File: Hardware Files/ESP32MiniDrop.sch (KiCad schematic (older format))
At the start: 51 parts, among them J1 USB_B_Mini, J2 Barrel_Jack, J3 AudioJack3, J4 Solenoid1 Terminal, J5 0.100\" 2x4 Header, M1 Conn_01x01, M2 Conn_01x01, M3 Conn_01x01, M4 Conn_01x01, Q1 S8050, Q2 S8050, Q3 NMOS 60V 46A, SW1 SPST (RED), SW2 SPST (BLUE), U1 CP2102N-A01-GQFN28, U2 AZ1117-3.3, U3 ESP32-WROOM-32, U4 4N25, U5 4N25

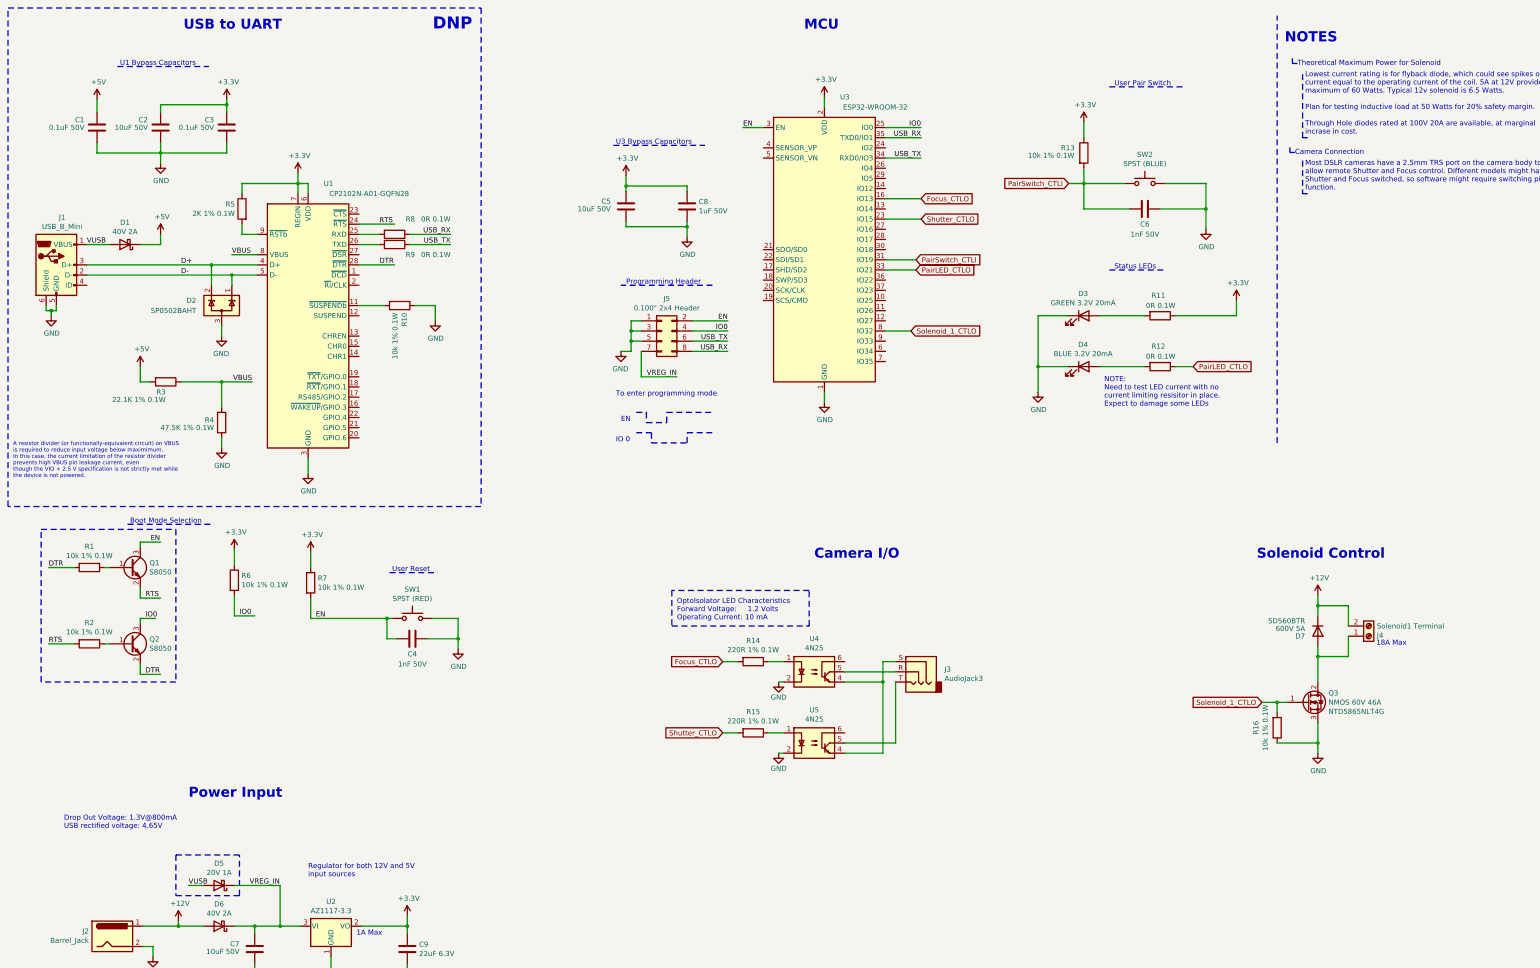
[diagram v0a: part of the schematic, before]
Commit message: Remove USB to UART components
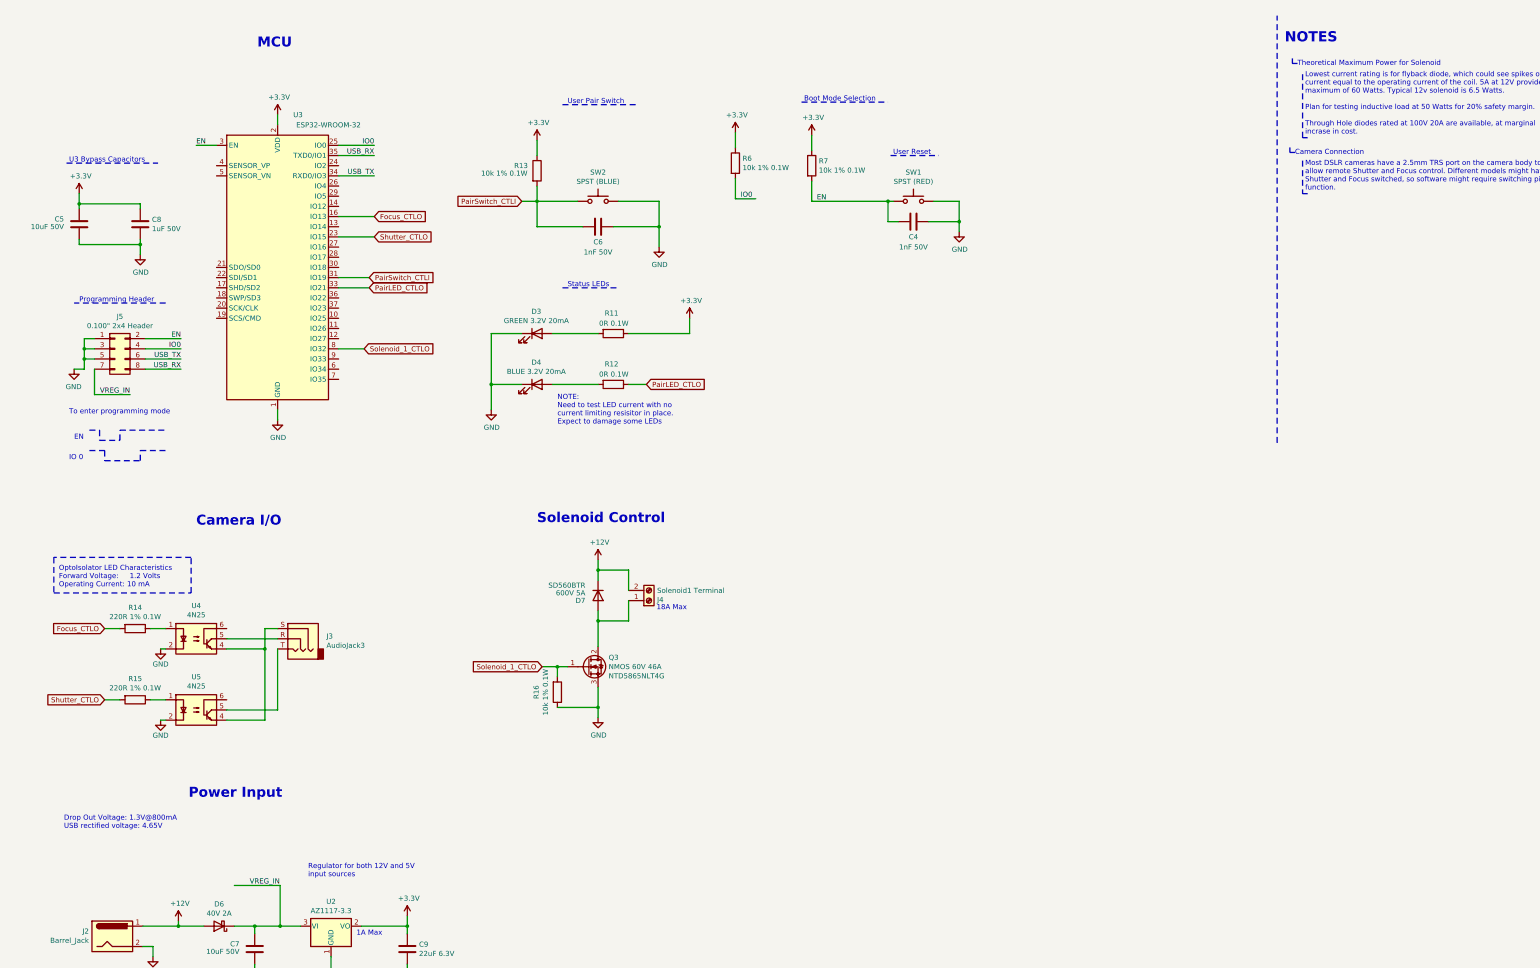
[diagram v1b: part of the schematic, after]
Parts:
- removed C1, C3: 0.1uF 50V, Capacitor_SMD:C_0603_1608Metric_Pad1.05x0.95mm_HandSolder, symbol Device:C
- removed C2: 10uF 50V, Capacitor_SMD:C_1206_3216Metric_Pad1.42x1.75mm_HandSolder, symbol Device:C
- removed D1: 40V 2A, Diode_SMD:D_SOD-123F, symbol Diode:1N5819
- removed D2: SP0502BAHT, Package_TO_SOT_SMD:SOT-23, symbol Power_Protection:SP0502BAHT
- removed D5: 20V 1A, Diode_SMD:D_SOD-123F, symbol Diode:1N5819
- removed J1: USB_B_Mini, ESP32 Drop Controller:USB_Micro-B_Molex-105017-0001_3D, symbol Connector:USB_B_Mini
- removed Q1, Q2: S8050, Package_TO_SOT_SMD:SOT-23, symbol Device:Q_NPN_BEC
- removed R1, R10, R2: 10k 1% 0.1W, Resistor_SMD:R_0603_1608Metric_Pad1.05x0.95mm_HandSolder, symbol Device:R
- removed R3: 22.1K 1% 0.1W, Resistor_SMD:R_0603_1608Metric_Pad1.05x0.95mm_HandSolder, symbol Device:R
- removed R4: 47.5K 1% 0.1W, Resistor_SMD:R_0603_1608Metric_Pad1.05x0.95mm_HandSolder, symbol Device:R
- removed R5: 2K 1% 0.1W, Resistor_SMD:R_0603_1608Metric_Pad1.05x0.95mm_HandSolder, symbol Device:R
- removed R8, R9: 0R 0.1W, Resistor_SMD:R_0603_1608Metric_Pad1.05x0.95mm_HandSolder, symbol Device:R
- removed U1: CP2102N-A01-GQFN28, Package_DFN_QFN:QFN-28-1EP_5x5mm_P0.5mm_EP3.35x3.35mm, symbol Interface_USB:CP2102N-A01-GQFN28
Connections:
- net labels removed: +5V, D+, D-, DTR, RTS, VBUS, VUSB
- wire segments 184 -> 120
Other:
- note removed: "A resistor divider (or functionally-equivalent circuit) on VBUS\nis required to reduce input voltage below maximimum. \nIn this case, the current limitation of the resistor divider \nprevents high VBUS pin leakage current, even \nthough the VIO + 2.5 V specification is not strictly met while\nthe device is not powered."
- note removed: "DNP"
- note removed: "U1 Bypass Capacitors"
- note removed: "USB to UART"
- moved on the sheet: C4, C5, C6, C8, D3, D4, D7, J3, J4, J5, Q3, R11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

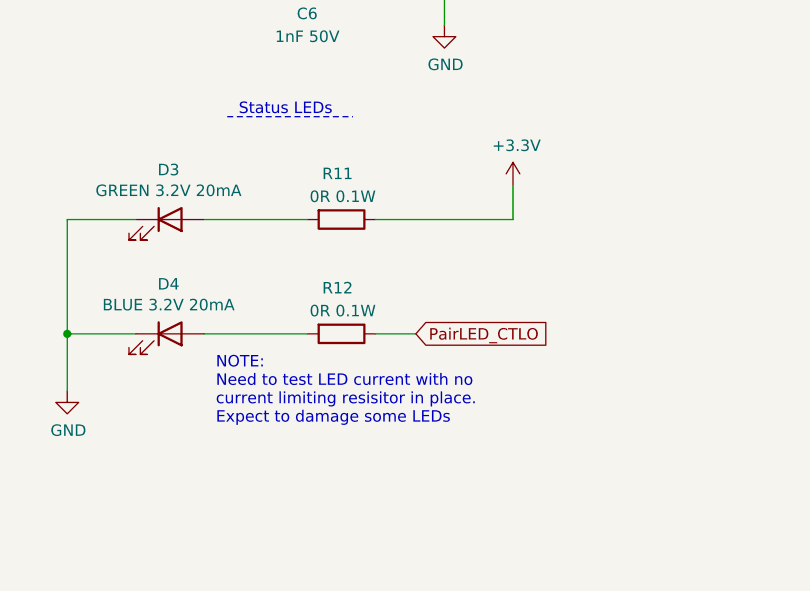
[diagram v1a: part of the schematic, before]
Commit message: Update passives to all 1206, unroute and reposition
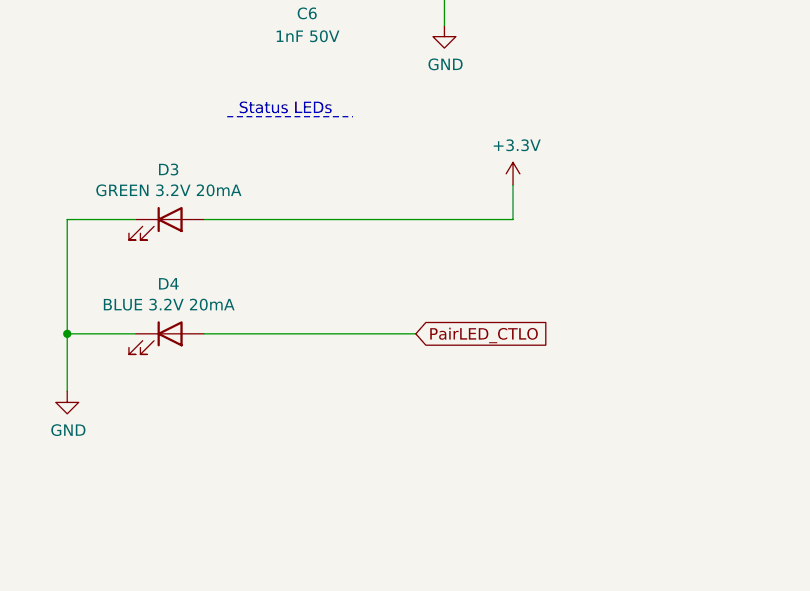
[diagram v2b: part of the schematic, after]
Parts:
- removed R11, R12: 0R 0.1W, Resistor_SMD:R_0603_1608Metric_Pad1.05x0.95mm_HandSolder, symbol Device:R
- C4, C6: footprint Capacitor_SMD:C_0603_1608Metric_Pad1.05x0.95mm_HandSolder -> Capacitor_SMD:C_1206_3216Metric_Pad1.42x1.75mm_HandSolder; MF Yageo -> (none); MPN CC0603KRX7R9BB102 -> (none)
- C8: footprint Capacitor_SMD:C_0603_1608Metric_Pad1.05x0.95mm_HandSolder -> Capacitor_SMD:C_1206_3216Metric_Pad1.42x1.75mm_HandSolder; MF Yageo -> (none); MPN CC0603KRX5R9BB105 -> (none)
- C9: footprint Capacitor_SMD:C_0805_2012Metric_Pad1.15x1.40mm_HandSolder -> Capacitor_SMD:C_1206_3216Metric_Pad1.42x1.75mm_HandSolder; MF Samsung Electro-Mechanics -> (none); MPN CL21A226MQQNNNE -> (none)
- R13, R16, R6, R7: footprint Resistor_SMD:R_0603_1608Metric_Pad1.05x0.95mm_HandSolder -> Resistor_SMD:R_1206_3216Metric_Pad1.42x1.75mm_HandSolder; MPN RC0603FR-0710KL -> (none)
- R14, R15: footprint Resistor_SMD:R_0603_1608Metric_Pad1.05x0.95mm_HandSolder -> Resistor_SMD:R_1206_3216Metric_Pad1.42x1.75mm_HandSolder; MPN RC0603FR-07220RL -> (none)
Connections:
- net +3V3: now also D3.2 (A)
- net PairLED_CTLO: now also D4.2 (A)
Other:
- note removed: "NOTE:\nNeed to test LED current with no\ncurrent limiting resisitor in place.\nExpect to damage some LEDs"
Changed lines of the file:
@@
 F 0 "R16" V 5718 7250 50  0000 C CNN
 F 1 "10k 1% 0.1W" V 5809 7250 50  0000 C CNN
-F 2 "Resistor_SMD:R_0603_1608Metric_Pad1.05x0.95mm_HandSolder" V 5855 7250 50  0001 C CNN
+F 2 "Resistor_SMD:R_1206_3216Metric_Pad1.42x1.75mm_HandSolder" V 5855 7250 50  0001 C CNN
 F 3 "~" H 5925 7250 50  0001 C CNN
 F 4 "Yageo" H 5925 7250 50  0001 C CNN "MF"
-F 5 "RC0603FR-0710KL" H 5925 7250 50  0001 C CNN "MPN"
+F 5 "" H 5925 7250 50  0001 C CNN "MPN"
 	1    5925 7250
 	1    0    0    1
@@
 F 0 "R6" H 7745 2096 50  0000 L CNN
 F 1 "10k 1% 0.1W" H 7745 2005 50  0000 L CNN
-F 2 "Resistor_SMD:R_0603_1608Metric_Pad1.05x0.95mm_HandSolder" V 7605 2050 50  0001 C CNN
+F 2 "Resistor_SMD:R_1206_3216Metric_Pad1.42x1.75mm_HandSolder" V 7605 2050 50  0001 C CNN
 F 3 "~" H 7675 2050 50  0001 C CNN
 F 4 "Yageo" H 7675 2050 50  0001 C CNN "MF"
-F 5 "RC0603FR-0710KL" H 7675 2050 50  0001 C CNN "MPN"
+F 5 "" H 7675 2050 50  0001 C CNN "MPN"
 	1    7675 2050
 	1    0    0    -1
@@
 F 0 "R7" H 8495 2121 50  0000 L CNN
 F 1 "10k 1% 0.1W" H 8495 2030 50  0000 L CNN
-F 2 "Resistor_SMD:R_0603_1608Metric_Pad1.05x0.95mm_HandSolder" V 8355 2075 50  0001 C CNN
+F 2 "Resistor_SMD:R_1206_3216Metric_Pad1.42x1.75mm_HandSolder" V 8355 2075 50  0001 C CNN
 F 3 "~" H 8425 2075 50  0001 C CNN
 F 4 "Yageo" H 8425 2075 50  0001 C CNN "MF"
-F 5 "RC0603FR-0710KL" H 8425 2075 50  0001 C CNN "MPN"
+F 5 "" H 8425 2075 50  0001 C CNN "MPN"
 	1    8425 2075
 	1    0    0    -1
@@
 F 0 "C8" H 1940 2696 50  0000 L CNN
 F 1 "1uF 50V" H 1940 2605 50  0000 L CNN
-F 2 "Capacitor_SMD:C_0603_1608Metric_Pad1.05x0.95mm_HandSolder" H 1863 2500 50  0001 C CNN
+F 2 "Capacitor_SMD:C_1206_3216Metric_Pad1.42x1.75mm_HandSolder" H 1863 2500 50  0001 C CNN
 F 3 "~" H 1825 2650 50  0001 C CNN
-F 4 "Yageo" H 1825 2650 50  0001 C CNN "MF"
-F 5 "CC0603KRX5R9BB105" H 1825 2650 50  0001 C CNN "MPN"
+F 4 "" H 1825 2650 50  0001 C CNN "MF"
+F 5 "" H 1825 2650 50  0001 C CNN "MPN"
 	1    1825 2650
 	1    0    0    -1
@@
 F 0 "C4" V 9575 2625 50  0000 C CNN
 F 1 "1nF 50V" V 9675 2625 50  0000 C CNN
-F 2 "Capacitor_SMD:C_0603_1608Metric_Pad1.05x0.95mm_HandSolder" H 9463 2475 50  0001 C CNN
+F 2 "Capacitor_SMD:C_1206_3216Metric_Pad1.42x1.75mm_HandSolder" H 9463 2475 50  0001 C CNN
 F 3 "~" H 9425 2625 50  0001 C CNN
-F 4 "Yageo" V 9425 2625 50  0001 C CNN "MF"
-F 5 "CC0603KRX7R9BB102" V 9425 2625 50  0001 C CNN "MPN"
+F 4 "" V 9425 2625 50  0001 C CNN "MF"
+F 5 "" V 9425 2625 50  0001 C CNN "MPN"
 	1    9425 2625
 	0    1    1    0
@@
 F 0 "C6" V 6475 2675 50  0000 C CNN
 F 1 "1nF 50V" V 6575 2675 50  0000 C CNN
-F 2 "Capacitor_SMD:C_0603_1608Metric_Pad1.05x0.95mm_HandSolder" H 6363 2525 50  0001 C CNN
+F 2 "Capacitor_SMD:C_1206_3216Metric_Pad1.42x1.75mm_HandSolder" H 6363 2525 50  0001 C CNN
 F 3 "~" H 6325 2675 50  0001 C CNN
-F 4 "Yageo" V 6325 2675 50  0001 C CNN "MF"
-F 5 "CC0603KRX7R9BB102" V 6325 2675 50  0001 C CNN "MPN"
+F 4 "" V 6325 2675 50  0001 C CNN "MF"
+F 5 "" V 6325 2675 50  0001 C CNN "MPN"
 	1    6325 2675
 	0    1    1    0
@@
 F 0 "R13" H 5500 2175 50  0000 L CNN
 F 1 "10k 1% 0.1W" H 5175 2100 50  0000 L CNN
-F 2 "Resistor_SMD:R_0603_1608Metric_Pad1.05x0.95mm_HandSolder" V 5655 2125 50  0001 C CNN
+F 2 "Resistor_SMD:R_1206_3216Metric_Pad1.42x1.75mm_HandSolder" V 5655 2125 50  0001 C CNN
 F 3 "~" H 5725 2125 50  0001 C CNN
 F 4 "Yageo" H 5725 2125 50  0001 C CNN "MF"
-F 5 "RC0603FR-0710KL" H 5725 2125 50  0001 C CNN "MPN"
+F 5 "" H 5725 2125 50  0001 C CNN "MPN"
 	1    5725 2125
 	1    0    0    -1
@@
 $EndComp
 Wire Wire Line
-	6325 3725 5875 3725
-Wire Wire Line
 	5575 3725 5275 3725
 Wire Wire Line
@@
 Wire Wire Line
 	3775 3175 4075 3175
-Wire Wire Line
-	5875 4225 6325 4225
 $Comp
 L Regulator_Linear:AZ1117-3.3 U?
@@
 F 0 "C9" H 4565 9821 50  0000 L CNN
 F 1 "22uF 6.3V" H 4565 9730 50  0000 L CNN
-F 2 "Capacitor_SMD:C_0805_2012Metric_Pad1.15x1.40mm_HandSolder" H 4488 9625 50  0001 C CNN
+F 2 "Capacitor_SMD:C_1206_3216Metric_Pad1.42x1.75mm_HandSolder" H 4488 9625 50  0001 C CNN
 F 3 "~" H 4450 9775 50  0001 C CNN
-F 4 "Samsung Electro-Mechanics" H 4450 9775 50  0001 C CNN "MF"
-F 5 "CL21A226MQQNNNE" H 4450 9775 50  0001 C CNN "MPN"
+F 4 "" H 4450 9775 50  0001 C CNN "MF"
+F 5 "" H 4450 9775 50  0001 C CNN "MPN"
 	1    4450 9775
 	1    0    0    -1
@@
 F 0 "R14" V 1568 6625 50  0000 C CNN
 F 1 "220R 1% 0.1W" V 1659 6625 50  0000 C CNN
-F 2 "Resistor_SMD:R_0603_1608Metric_Pad1.05x0.95mm_HandSolder" V 1705 6625 50  0001 C CNN
+F 2 "Resistor_SMD:R_1206_3216Metric_Pad1.42x1.75mm_HandSolder" V 1705 6625 50  0001 C CNN
 F 3 "~" H 1775 6625 50  0001 C CNN
 F 4 "Yageo" H 1775 6625 50  0001 C CNN "MF"
-F 5 "RC0603FR-07220RL" H 1775 6625 50  0001 C CNN "MPN"
+F 5 "" H 1775 6625 50  0001 C CNN "MPN"
 	1    1775 6625
 	0    1    1    0
@@
 F 0 "R15" V 1568 7325 50  0000 C CNN
 F 1 "220R 1% 0.1W" V 1659 7325 50  0000 C CNN
-F 2 "Resistor_SMD:R_0603_1608Metric_Pad1.05x0.95mm_HandSolder" V 1705 7325 50  0001 C CNN
+F 2 "Resistor_SMD:R_1206_3216Metric_Pad1.42x1.75mm_HandSolder" V 1705 7325 50  0001 C CNN
 F 3 "~" H 1775 7325 50  0001 C CNN
 F 4 "Yageo" H 1775 7325 50  0001 C CNN "MF"
-F 5 "RC0603FR-07220RL" H 1775 7325 50  0001 C CNN "MPN"
+F 5 "" H 1775 7325 50  0001 C CNN "MPN"
 	1    1775 7325
 	0    1    1    0
@@
 Wire Notes Line style solid
 	2325 5925 975  5925
-$Comp
-L Device:R R?
-U 1 1 5F65878C
-P 6475 3725
-AR Path="/5F45F2B5/5F65878C" Ref="R?"  Part="1"
-AR Path="/5F65878C" Ref="R11"  Part="1"
-F 0 "R11" V 6275 3775 50  0000 R CNN
-F 1 "0R 0.1W" V 6375 3875 50  0000 R CNN
-F 2 "Resistor_SMD:R_0603_1608Metric_Pad1.05x0.95mm_HandSolder" V 6405 3725 50  0001 C CNN
-F 3 "~" H 6475 3725 50  0001 C CNN
-F 4 "Yageo" H 6475 3725 50  0001 C CNN "MF"
-F 5 "311-0.0GRCT-ND" H 6475 3725 50  0001 C CNN "MPN"
-	1    6475 3725
-	0    1    1    0
-$EndComp
-$Comp
-L Device:R R?
-U 1 1 5F6593F1
-P 6475 4225
-AR Path="/5F45F2B5/5F6593F1" Ref="R?"  Part="1"
-AR Path="/5F6593F1" Ref="R12"  Part="1"
-F 0 "R12" V 6275 4275 50  0000 R CNN
-F 1 "0R 0.1W" V 6375 4375 50  0000 R CNN
-F 2 "Resistor_SMD:R_0603_1608Metric_Pad1.05x0.95mm_HandSolder" V 6405 4225 50  0001 C CNN
-F 3 "~" H 6475 4225 50  0001 C CNN
-F 4 "Yageo" H 6475 4225 50  0001 C CNN "MF"
-F 5 "311-0.0GRCT-ND" H 6475 4225 50  0001 C CNN "MPN"
-	1    6475 4225
-	0    1    1    0
-$EndComp
 $Comp
 L Connector_Generic:Conn_02x04_Odd_Even J5
@@
 	1100 2050 2000 2050
 Wire Wire Line
-	6625 3725 7225 3725
-Wire Wire Line
 	7225 3575 7225 3725
 Text Notes 6025 3275 0    50   ~ 0
@@
 Text GLabel 6800 4225 2    50   Input ~ 0
 PairLED_CTLO
-Wire Wire Line
-	6625 4225 6800 4225
 Text Notes 13075 875  0    100  ~ 20
 NOTES
@@
 Wire Notes Line
 	9200 1975 9675 1975
-Text Notes 5925 4625 0    50   ~ 0
-NOTE:\nNeed to test LED current with no\ncurrent limiting resisitor in place.\nExpect to damage some LEDs
 Wire Wire Line
 	3050 7525 3050 6825
@@
 Wire Wire Line
 	4125 1875 3775 1875
+Wire Wire Line
+	5875 3725 7225 3725
+Wire Wire Line
+	5875 4225 6800 4225
 $EndSCHEMATC
